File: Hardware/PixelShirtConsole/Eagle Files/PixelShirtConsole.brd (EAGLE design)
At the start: 50 x 50 mm, 7 parts

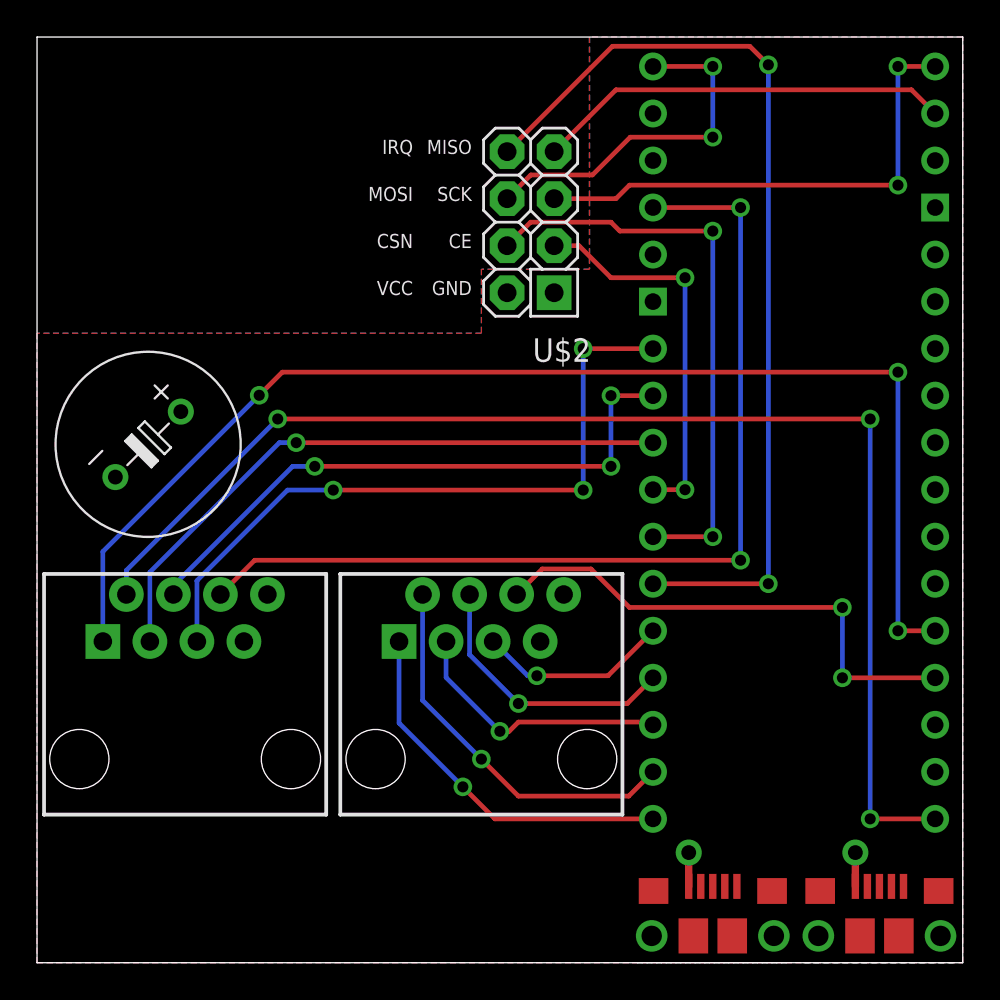
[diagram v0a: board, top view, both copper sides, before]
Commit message: Moved some parts around for clearance Added logo, name Added Gerber files
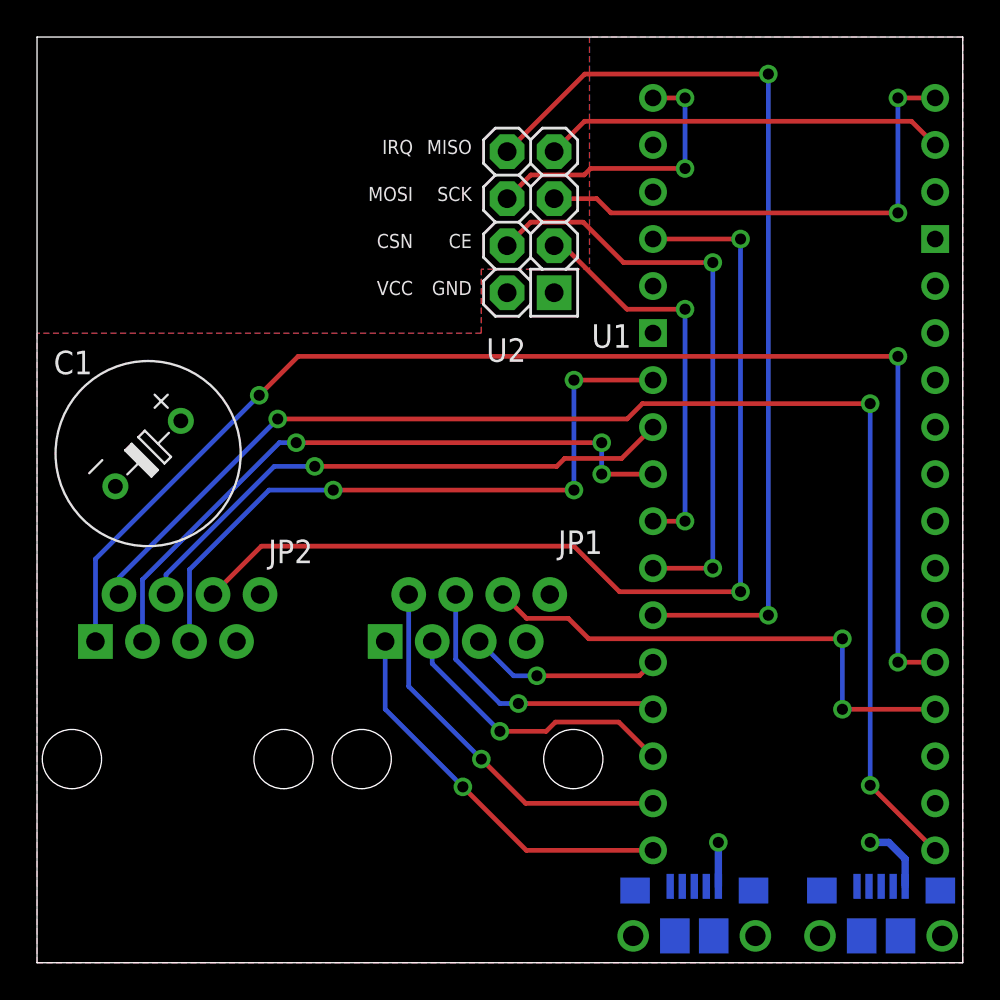
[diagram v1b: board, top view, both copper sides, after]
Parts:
- removed U$1: ARDUINO_MICROFOOTPRINT, arduino-micro:ARDUINO-MICRO
- removed U$3, U$4: USB-MICRO-B, usb:USB-MICRO-B
- added JP3, JP4: USB-MICRO-B, usb:USB-MICRO-B
- added U1: ARDUINO_MICROFOOTPRINT, arduino-micro:ARDUINO-MICRO
- C1: value CAP-CUSTOM -> 1000µF
- moved JP1 0.75 mm to (23.2, 11.0)
- moved C1 0.50 mm to (6.00, 27.5)
- moved JP2 0.40 mm to (7.60, 11.0)
- renumbered U$2 to U2
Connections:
- net GND: now also JP3.GND@1, JP3.GND@2, JP3.GND@3, JP3.GND@5, JP3.GND@6, JP3.GND@7, JP3.GNF@4, JP4.GND@1, JP4.GND@2, JP4.GND@3, JP4.GND@5, JP4.GND@6, JP4.GND@7, JP4.GNF@4, U1.GND, U1.GND1; no longer U$1.GND, U$1.GND1, U$3.GND@1, U$3.GND@2, U$3.GND@3, U$3.GND@5, U$3.GND@6, U$3.GND@7, U$3.GNF@4, U$4.GND@1, U$4.GND@2, U$4.GND@3, U$4.GND@5, U$4.GND@6, U$4.GND@7, U$4.GNF@4
- net N$1: now also U1.MISO; no longer U$1.MISO
- net N$10: now also U1.D12; no longer U$1.D12
- net N$11: now also U1.A0; no longer U$1.A0
- net N$12: now also U1.D8; no longer U$1.D8
- net N$13: now also U1.D2; no longer U$1.D2
- net N$14: now also U1.D3; no longer U$1.D3
- net N$15: now also U1.D4; no longer U$1.D4
- net N$16: now also U1.RX; no longer U$1.RX
- net N$17: now also U1.A1; no longer U$1.A1
- net N$18: now also U1.D13; no longer U$1.D13
- net N$2: now also U1.SCK; no longer U$1.SCK
- net N$3: now also U1.D6; no longer U$1.D6
- net N$4: now also U1.D5; no longer U$1.D5
- net N$5: now also U1.MOSI; no longer U$1.MOSI
- net N$6: now also U1.D7; no longer U$1.D7
- net N$7: now also U1.D11; no longer U$1.D11
- net N$8: now also U1.D10; no longer U$1.D10
- net N$9: now also U1.D9; no longer U$1.D9
- net VCC: now also JP3.VCC@1, JP4.VCC@1, U1.VIN; no longer U$1.VIN, U$3.VCC@1, U$3.VCC@2, U$4.VCC@1, U$4.VCC@2
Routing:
- net VCC: track 0.00 -> 6.12 mm, vias 0 -> 2
- net N$5: track 19.5 -> 15.8 mm
- net N$17: track 67.8 -> 70.9 mm
- net N$14: track 32.9 -> 30.7 mm, vias 3 -> 1
- net N$15: track 33.8 -> 35.7 mm, vias 1 -> 3
- net N$16: track 52.6 -> 54.4 mm
- net N$8: track 14.6 -> 15.6 mm
- net N$10: track 20.3 -> 21.3 mm
- net N$18: track 70.0 -> 71.0 mm
- net N$13: track 37.6 -> 36.6 mm
- net N$3: track 31.6 -> 32.3 mm
- net N$4: track 21.0 -> 21.7 mm
- net N$1: track 22.5 -> 21.8 mm
- added copper zone on layer 16, net GND
- added copper zone on layer 1, net VCC
- removed copper zone on layer 1, net GND
- removed copper zone on layer 16, net VCC
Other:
- board text added: "Adam Feinstein (C) 2015"
- board text added: "Os - 12 O - 11 Gs - 10 U - 9 Us - 8 G - A0 Bs - GND B - VCC"
- board text added: "Os - A1 O - 13 Gs - 4 U - 3 Us - 2 G - 0 Bs - GND B - VCC"

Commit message: Modified pin definitions for new board Fixed schematic issue where the nRF had 5V powering it instead of 3.3V
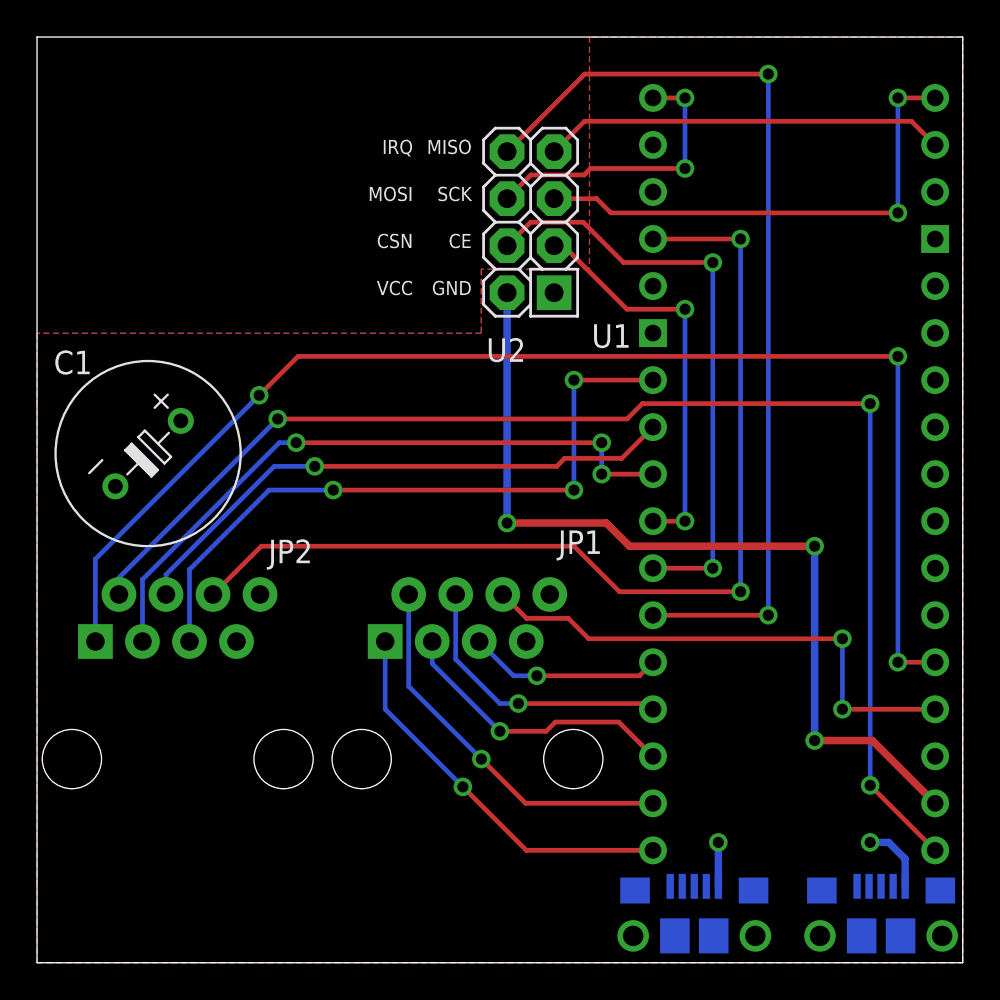
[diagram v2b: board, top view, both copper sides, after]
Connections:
- new net N$19: U1.3V3, U2.VCC
- net VCC: no longer U2.VCC
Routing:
- net N$19: track 0.00 -> 48.0 mm, vias 0 -> 3
